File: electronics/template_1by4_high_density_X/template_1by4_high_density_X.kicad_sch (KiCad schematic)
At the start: 12 parts, among them J1 1, J10 10, J2 2, J3 3, J4 4, J5 5, J6 6, J7 7, J8 8, J9 9

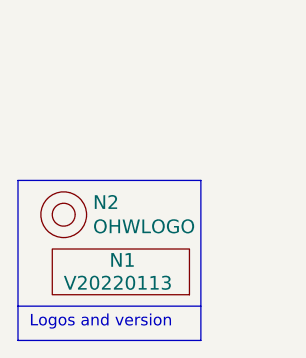
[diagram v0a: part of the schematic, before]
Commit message: completed high density X templates, updated versionnumbers of high density XN templates
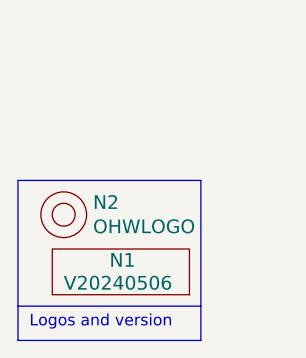
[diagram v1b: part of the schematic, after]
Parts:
- N1: value V20220113 -> V20240506
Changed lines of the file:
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@@
       (effects (font (size 1.524 1.524)) (justify left))
     )
-    (property "Value" "V20220113" (at 20.32 189.23 0)
+    (property "Value" "V20240506" (at 20.32 189.23 0)
       (effects (font (size 1.524 1.524)) (justify left))
     )
@@
     )
     (instances
-      (project "template_1by4"
+      (project "template_1by4_high_density_X"
         (path "/4afa80ff-4542-4837-ba2e-ef55b455ed28"
           (reference "N1") (unit 1)
@@
     )
     (instances
-      (project "template_1by4"
+      (project "template_1by4_high_density_X"
         (path "/4afa80ff-4542-4837-ba2e-ef55b455ed28"
           (reference "N2") (unit 1)
@@
     (pin "1")
     (instances
-      (project "template_1by4"
+      (project "template_1by4_high_density_X"
         (path "/4afa80ff-4542-4837-ba2e-ef55b455ed28"
           (reference "J2") (unit 1)
@@
     (pin "1")
     (instances
-      (project "template_1by4"
+      (project "template_1by4_high_density_X"
         (path "/4afa80ff-4542-4837-ba2e-ef55b455ed28"
           (reference "J1") (unit 1)
@@
     (pin "1")
     (instances
-      (project "template_1by4"
+      (project "template_1by4_high_density_X"
         (path "/4afa80ff-4542-4837-ba2e-ef55b455ed28"
           (reference "J3") (unit 1)
@@
     (pin "1")
     (instances
-      (project "template_1by4"
+      (project "template_1by4_high_density_X"
         (path "/4afa80ff-4542-4837-ba2e-ef55b455ed28"
           (reference "J4") (unit 1)
@@
     (pin "1")
     (instances
-      (project "template_1by4"
+      (project "template_1by4_high_density_X"
         (path "/4afa80ff-4542-4837-ba2e-ef55b455ed28"
           (reference "J5") (unit 1)
@@
     (pin "1")
     (instances
-      (project "template_1by4"
+      (project "template_1by4_high_density_X"
         (path "/4afa80ff-4542-4837-ba2e-ef55b455ed28"
           (reference "J6") (unit 1)
@@
     (pin "1")
     (instances
-      (project "template_1by4"
+      (project "template_1by4_high_density_X"
         (path "/4afa80ff-4542-4837-ba2e-ef55b455ed28"
           (reference "J9") (unit 1)
@@
     (pin "1")
     (instances
-      (project "template_1by4"
+      (project "template_1by4_high_density_X"
         (path "/4afa80ff-4542-4837-ba2e-ef55b455ed28"
           (reference "J7") (unit 1)
@@
     (pin "1")
     (instances
-      (project "template_1by4"
+      (project "template_1by4_high_density_X"
         (path "/4afa80ff-4542-4837-ba2e-ef55b455ed28"
           (reference "J8") (unit 1)
@@
     (pin "1")
     (instances
-      (project "template_1by4"
+      (project "template_1by4_high_density_X"
         (path "/4afa80ff-4542-4837-ba2e-ef55b455ed28"
           (reference "J10") (unit 1)
